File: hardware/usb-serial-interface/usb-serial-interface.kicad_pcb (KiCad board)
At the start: 2 copper layers, 51.4 x 36.2 mm, 18 parts, among them J1 USB_B, J2 RJ12, U1 CP2102N-A01-GQFN24

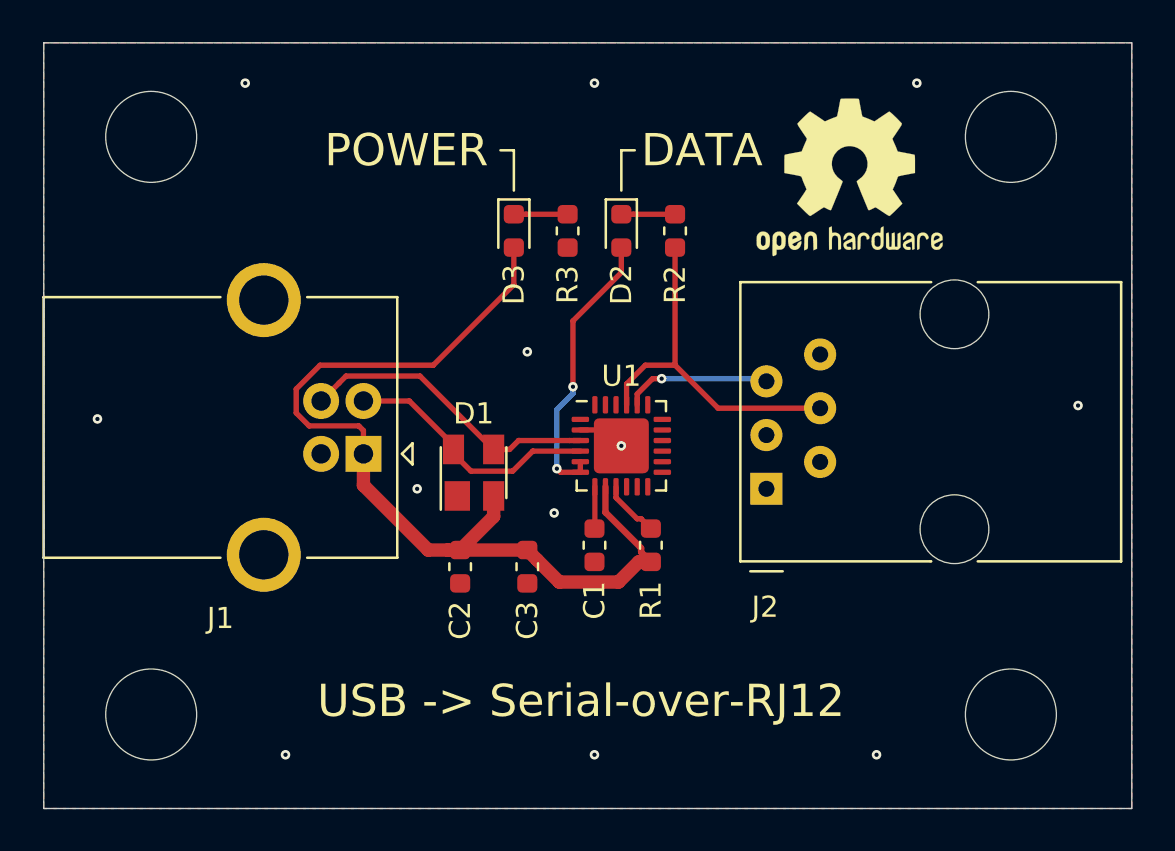
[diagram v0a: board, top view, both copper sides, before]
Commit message: Made v2 of serial interface + panelized
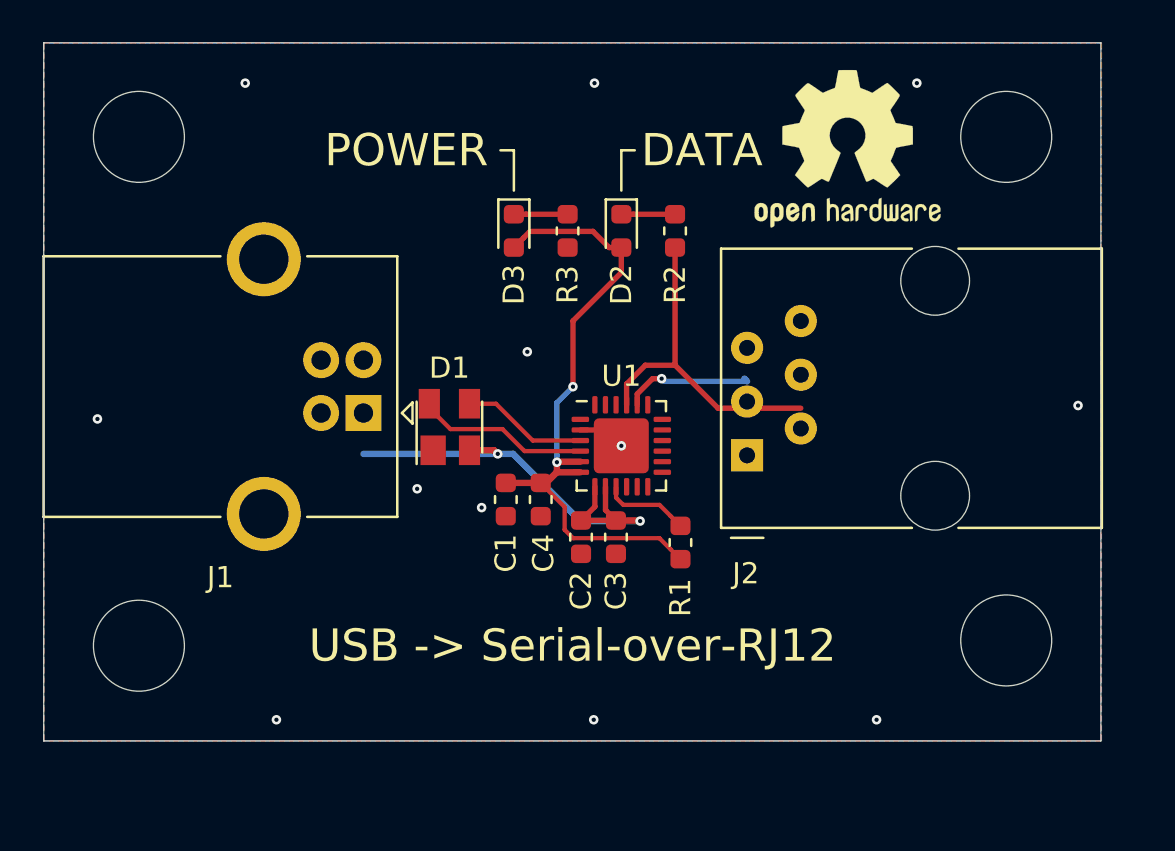
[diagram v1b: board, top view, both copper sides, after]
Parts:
- added C4: 0.1u, Capacitor_SMD:C_0603_1608Metric, F.Cu at (102.9, 85.7)
- C1: value 0.1u -> 4.7u
- C2: value 10u -> 4.7u
- moved C2 5.88 mm to (104.8, 87.5)
- moved C1 4.71 mm to (101.2, 85.7)
- moved C3 4.42 mm to (106.4, 87.5)
- moved REF** 3.51 mm to (124.9, 92.4)
- moved REF** 3.30 mm to (83.9, 92.6)
- moved D1 2.44 mm to (98.6, 82.3)
- moved J1 1.93 mm to (94.5, 81.6)
- moved J2 1.83 mm to (112.6, 83.6)
- moved R1 1.40 mm to (109.5, 87.8)
- moved REF** 1.35 mm to (117.4, 69.1)
- moved REF** 0.58 mm to (83.9, 68.6)
- moved REF** 0.22 mm to (124.9, 68.6)
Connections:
- C1 pad 1: Net-(C1-Pad1) -> +3V3
- D2 pad 2: VCC -> +3V3
- D3 pad 2: VBUS -> +3V3
- R1 pad 1: VBUS -> +3V3
- U1 pad 5: VCC -> +3V3
- U1 pad 6: VCC -> +3V3
- U1 pad 7: Net-(C1-Pad1) -> VBUS
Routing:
- net +3V3: track 0.00 -> 31.6 mm, vias 0 -> 2
- net VBUS: track 44.9 -> 22.3 mm, vias 0 -> 2
- net VCC: track 13.4 -> 0.00 mm, vias 2 -> 0
- net /D+: track 14.4 -> 5.96 mm
- net /D-: track 12.3 -> 8.19 mm
- net Net-(C1-Pad1): track 1.98 -> 0.00 mm
- net Net-(R1-Pad2): track 2.76 -> 4.11 mm
- net /TXD: track 16.9 -> 16.0 mm
- net /RXD: track 6.97 -> 6.24 mm
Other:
- board size 51.4 x 36.2 mm -> 50 x 33 mm
- board text added: "Willem Hillier rev2 19.222"
- board text removed: "Willem Hillier rev1 19.209"

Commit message: New USB to serial board image
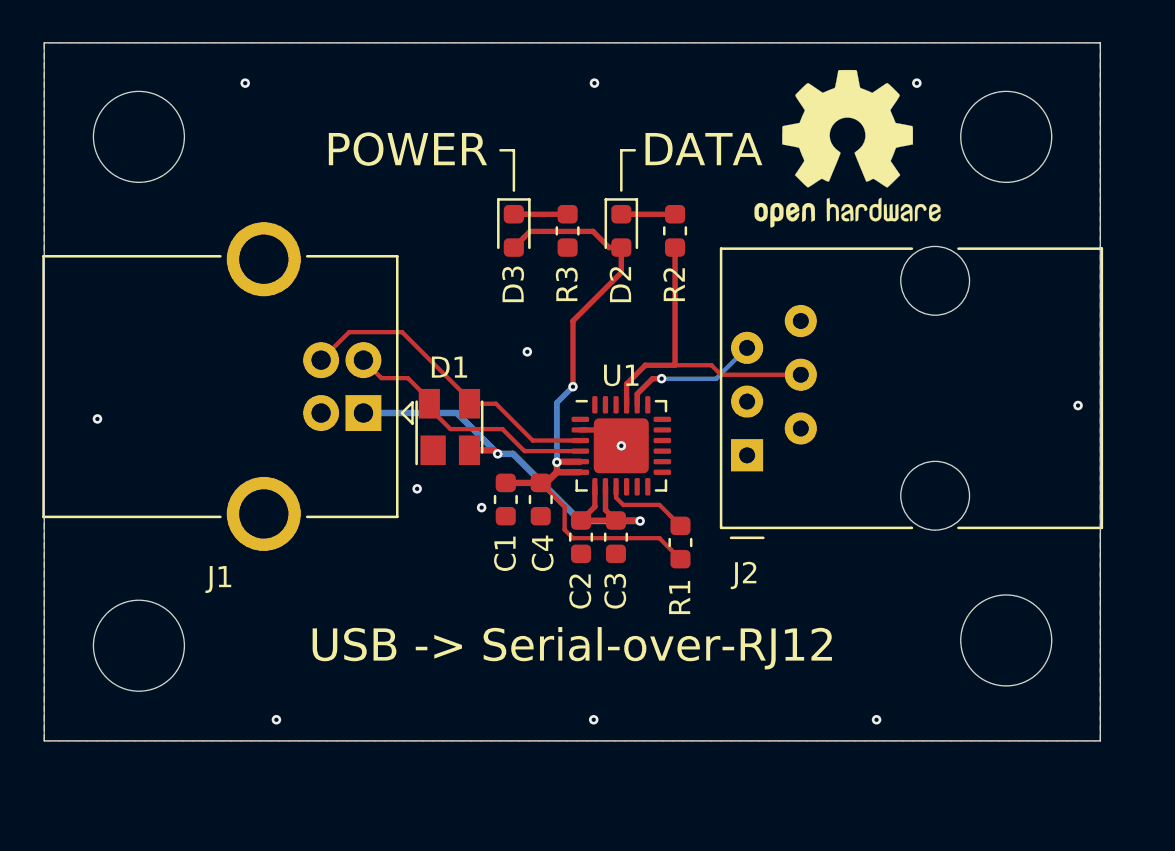
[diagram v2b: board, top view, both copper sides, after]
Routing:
- net /D+: track 5.96 -> 15.0 mm
- net /D-: track 8.19 -> 12.3 mm
- net VBUS: track 22.3 -> 23.1 mm
- net /TXD: track 16.0 -> 15.3 mm
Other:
- board size 50 x 33 mm -> 49.9 x 33 mm
- board text added: "Willem Hillier rev2.1 19.224"
- board text removed: "Willem Hillier rev2 19.222"
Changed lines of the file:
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@@
     (thickness 1.6)
     (drawings 16)
-    (tracks 86)
+    (tracks 96)
     (zones 0)
     (modules 19)
@@
   )
   (setup
-    (last_trace_width 0.254)
+    (last_trace_width 0.25)
     (user_trace_width 0.2032)
     (user_trace_width 0.254)
@@
     (effects (font (size 1.27 1.27) (thickness 0.1524)) (justify mirror))
   )
-  (gr_text "Willem Hillier rev2 19.222" (at 104.775 71.235) (layer B.SilkS)
+  (gr_text "Willem Hillier rev2.1 19.224" (at 104.775 71.235) (layer B.SilkS)
     (effects (font (size 1.524 1.524) (thickness 0.1778)) (justify mirror))
   )
@@
     (arrow2b (pts (xy 79.375 60.96) (xy 80.501504 60.373579)))
   )
-  (gr_line (start 129.35 97.135) (end 79.375 97.135) (layer Edge.Cuts) (width 0.05))
-  (gr_line (start 129.35 64.135) (end 129.35 97.135) (layer Edge.Cuts) (width 0.05))
-  (gr_line (start 79.375 64.135) (end 129.35 64.135) (layer Edge.Cuts) (width 0.05))
-  (gr_line (start 79.375 97.135) (end 79.375 64.135) (layer Edge.Cuts) (width 0.05))
+  (gr_line (start 129.325 97.135) (end 79.4 97.135) (layer Edge.Cuts) (width 0.05))
+  (gr_line (start 129.325 64.135) (end 129.325 97.135) (layer Edge.Cuts) (width 0.05))
+  (gr_line (start 79.4 64.135) (end 129.325 64.135) (layer Edge.Cuts) (width 0.05))
+  (gr_line (start 79.4 97.135) (end 79.4 64.135) (layer Edge.Cuts) (width 0.05))
   (via (at 100.076 86.106) (size 0.45) (drill 0.2) (layers F.Cu B.Cu) (net 1))
   (via (at 88.9 66.04) (size 0.45) (drill 0.2) (layers F.Cu B.Cu) (net 1))
@@
   (segment (start 104.775 86.7155) (end 106.426 86.7155) (width 0.254) (layer F.Cu) (net 2))
   (segment (start 101.565554 83.566) (end 104.740554 86.741) (width 0.3048) (layer B.Cu) (net 2))
-  (segment (start 94.488 83.566) (end 100.838 83.566) (width 0.3048) (layer B.Cu) (net 2))
   (segment (start 104.740554 86.741) (end 107.569 86.741) (width 0.3048) (layer B.Cu) (net 2))
   (segment (start 107.569 86.741) (end 107.569 86.741) (width 0.3048) (layer B.Cu) (net 2))
@@
   (segment (start 100.668 83.396) (end 100.838 83.566) (width 0.3048) (layer F.Cu) (net 2))
   (segment (start 99.502 83.396) (end 100.668 83.396) (width 0.3048) (layer F.Cu) (net 2))
+  (segment (start 98.907 81.635) (end 100.838 83.566) (width 0.3048) (layer B.Cu) (net 2))
+  (segment (start 94.488 81.635) (end 98.907 81.635) (width 0.3048) (layer B.Cu) (net 2))
   (segment (start 104.7425 82.935) (end 102.493 82.935) (width 0.2032) (layer F.Cu) (net 3))
   (segment (start 100.754 81.196) (end 99.502 81.196) (width 0.2032) (layer F.Cu) (net 3))
   (segment (start 102.493 82.935) (end 100.754 81.196) (width 0.2032) (layer F.Cu) (net 3))
+  (segment (start 99.502 80.996) (end 99.502 81.196) (width 0.2032) (layer F.Cu) (net 3))
+  (segment (start 93.813 77.81) (end 96.316 77.81) (width 0.2032) (layer F.Cu) (net 3))
+  (segment (start 96.316 77.81) (end 99.502 80.996) (width 0.2032) (layer F.Cu) (net 3))
+  (segment (start 92.488 79.135) (end 93.813 77.81) (width 0.2032) (layer F.Cu) (net 3))
   (segment (start 102.104 83.435) (end 104.7425 83.435) (width 0.2032) (layer F.Cu) (net 4))
   (segment (start 97.602 81.196) (end 97.602 81.396) (width 0.2032) (layer F.Cu) (net 4))
@@
   (segment (start 98.600399 82.394399) (end 101.063399 82.394399) (width 0.2032) (layer F.Cu) (net 4))
   (segment (start 101.063399 82.394399) (end 102.104 83.435) (width 0.2032) (layer F.Cu) (net 4))
+  (segment (start 97.602 80.996) (end 97.602 81.196) (width 0.2032) (layer F.Cu) (net 4))
+  (segment (start 95.337999 79.984999) (end 96.590999 79.984999) (width 0.2032) (layer F.Cu) (net 4))
+  (segment (start 96.590999 79.984999) (end 97.602 80.996) (width 0.2032) (layer F.Cu) (net 4))
+  (segment (start 94.488 79.135) (end 95.337999 79.984999) (width 0.2032) (layer F.Cu) (net 4))
   (segment (start 107.255 72.2375) (end 109.22 72.2375) (width 0.254) (layer F.Cu) (net 5) (status 20))
   (segment (start 106.68 72.2375) (end 107.255 72.2375) (width 0.254) (layer F.Cu) (net 5) (status 10))
@@
   (segment (start 107.815 79.375) (end 109.22 79.375) (width 0.254) (layer F.Cu) (net 7))
   (segment (start 109.22 73.8125) (end 109.22 79.375) (width 0.254) (layer F.Cu) (net 7) (status 10))
-  (segment (start 111.252 81.407) (end 115.165 81.407) (width 0.254) (layer F.Cu) (net 7))
-  (segment (start 109.22 79.375) (end 111.252 81.407) (width 0.254) (layer F.Cu) (net 7))
+  (segment (start 109.22 79.375) (end 110.94 79.375) (width 0.2032) (layer F.Cu) (net 7))
+  (segment (start 111.39 79.825) (end 115.165 79.825) (width 0.2032) (layer F.Cu) (net 7))
+  (segment (start 110.94 79.375) (end 111.39 79.825) (width 0.2032) (layer F.Cu) (net 7))
   (segment (start 106.77139 85.97639) (end 108.48089 85.97639) (width 0.2032) (layer F.Cu) (net 8))
   (segment (start 109.012388 86.507888) (end 109.474 86.9695) (width 0.2032) (layer F.Cu) (net 8))
@@
   (segment (start 108.155 80.01) (end 108.585 80.01) (width 0.254) (layer F.Cu) (net 9))
   (via (at 108.585 80.01) (size 0.45) (drill 0.2) (layers F.Cu B.Cu) (net 9))
-  (segment (start 112.498 80.01) (end 112.625 80.137) (width 0.3048) (layer B.Cu) (net 9))
-  (segment (start 108.712 80.137) (end 108.585 80.01) (width 0.254) (layer B.Cu) (net 9))
-  (segment (start 112.625 80.137) (end 108.712 80.137) (width 0.254) (layer B.Cu) (net 9))
+  (segment (start 111.47 79.71) (end 112.625 78.555) (width 0.2032) (layer B.Cu) (net 9))
+  (segment (start 111.17 80.01) (end 111.47 79.71) (width 0.2032) (layer B.Cu) (net 9))
+  (segment (start 108.585 80.01) (end 111.17 80.01) (width 0.2032) (layer B.Cu) (net 9))
   (segment (start 102.36451 73.04799) (end 102.061612 73.350888) (width 0.254) (layer F.Cu) (net 10))
   (segment (start 105.34049 73.04799) (end 102.36451 73.04799) (width 0.254) (layer F.Cu) (net 10))
@@
     (polygon
       (pts
-        (xy 79.375 64.135) (xy 129.375 64.135) (xy 129.35 97.135) (xy 79.375 97.135)
+        (xy 79.4 64.135) (xy 129.325 64.135) (xy 129.325 97.135) (xy 79.4 97.135)
       )
     )
@@
     (polygon
       (pts
-        (xy 79.375 97.135) (xy 129.375 97.135) (xy 129.375 64.135) (xy 79.375 64.135)
+        (xy 79.4 97.135) (xy 129.325 97.135) (xy 129.325 64.135) (xy 79.4 64.135)
       )
     )
